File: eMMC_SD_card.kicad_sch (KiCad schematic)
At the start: 2 parts

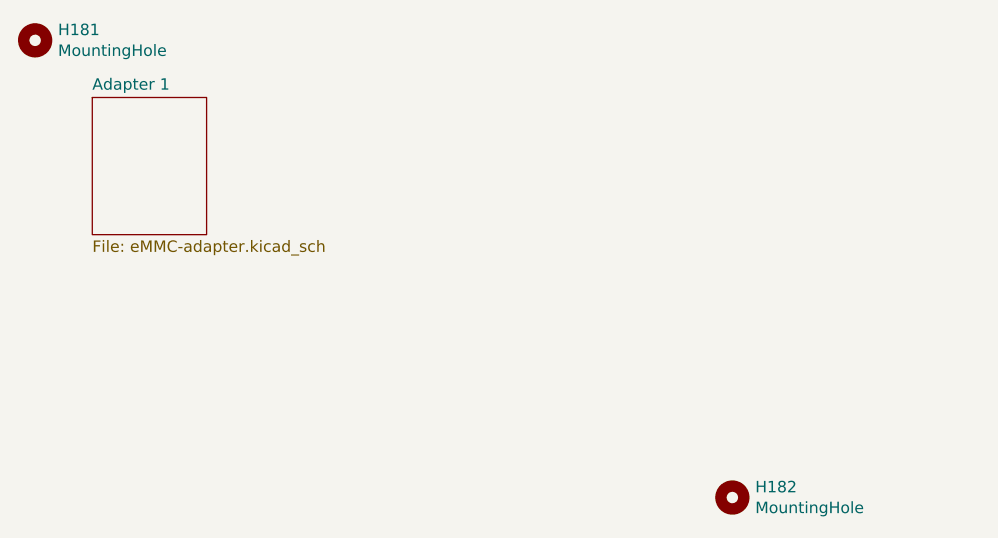
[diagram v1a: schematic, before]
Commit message: Panelize
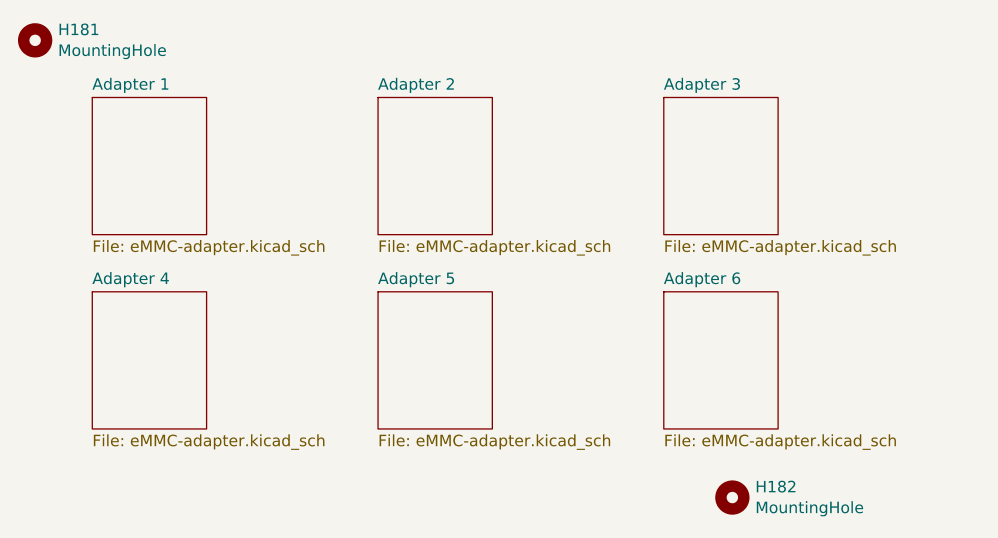
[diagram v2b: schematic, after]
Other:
- added sheet Adapter 2 (eMMC-adapter.kicad_sch)
- added sheet Adapter 3 (eMMC-adapter.kicad_sch)
- added sheet Adapter 4 (eMMC-adapter.kicad_sch)
- added sheet Adapter 5 (eMMC-adapter.kicad_sch)
- added sheet Adapter 6 (eMMC-adapter.kicad_sch)
